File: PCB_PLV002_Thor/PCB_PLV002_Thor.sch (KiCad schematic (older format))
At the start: 24 parts, among them J1 Conn_01x12, U1 R-78B12-2.0, U2 LM317DCYRG3, U3 SN65HVD232

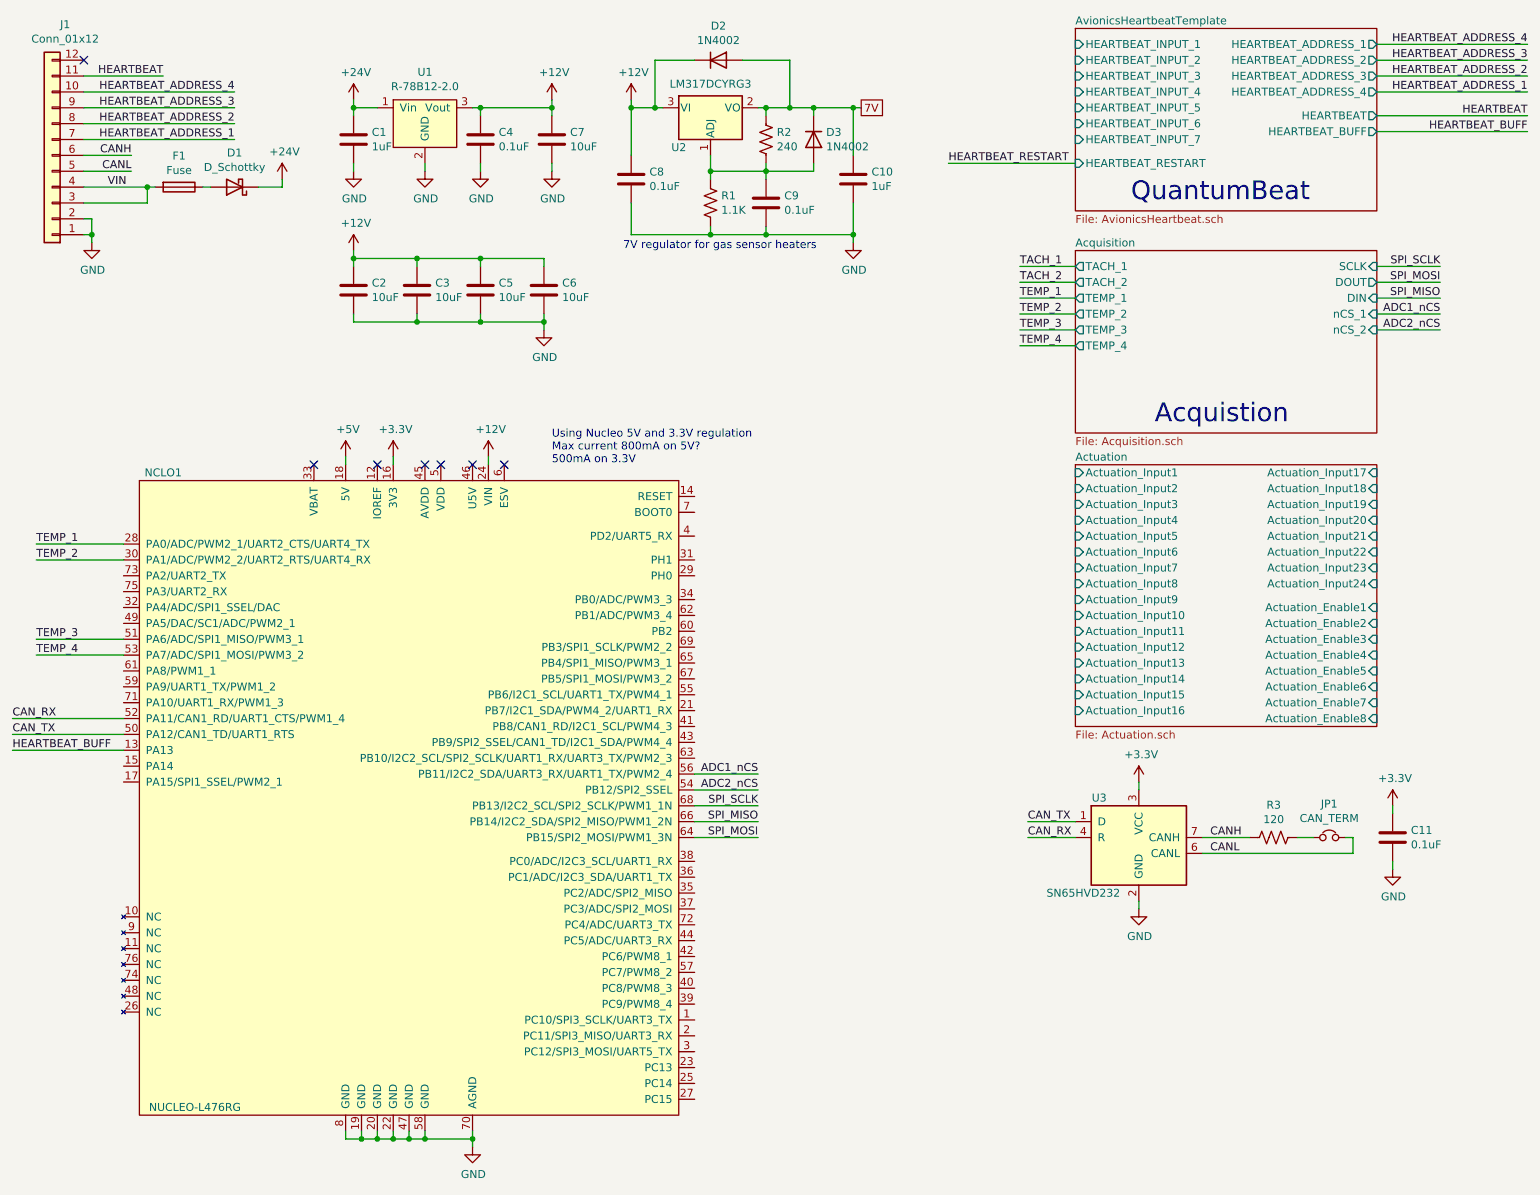
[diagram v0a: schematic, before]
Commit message: Finish schematic
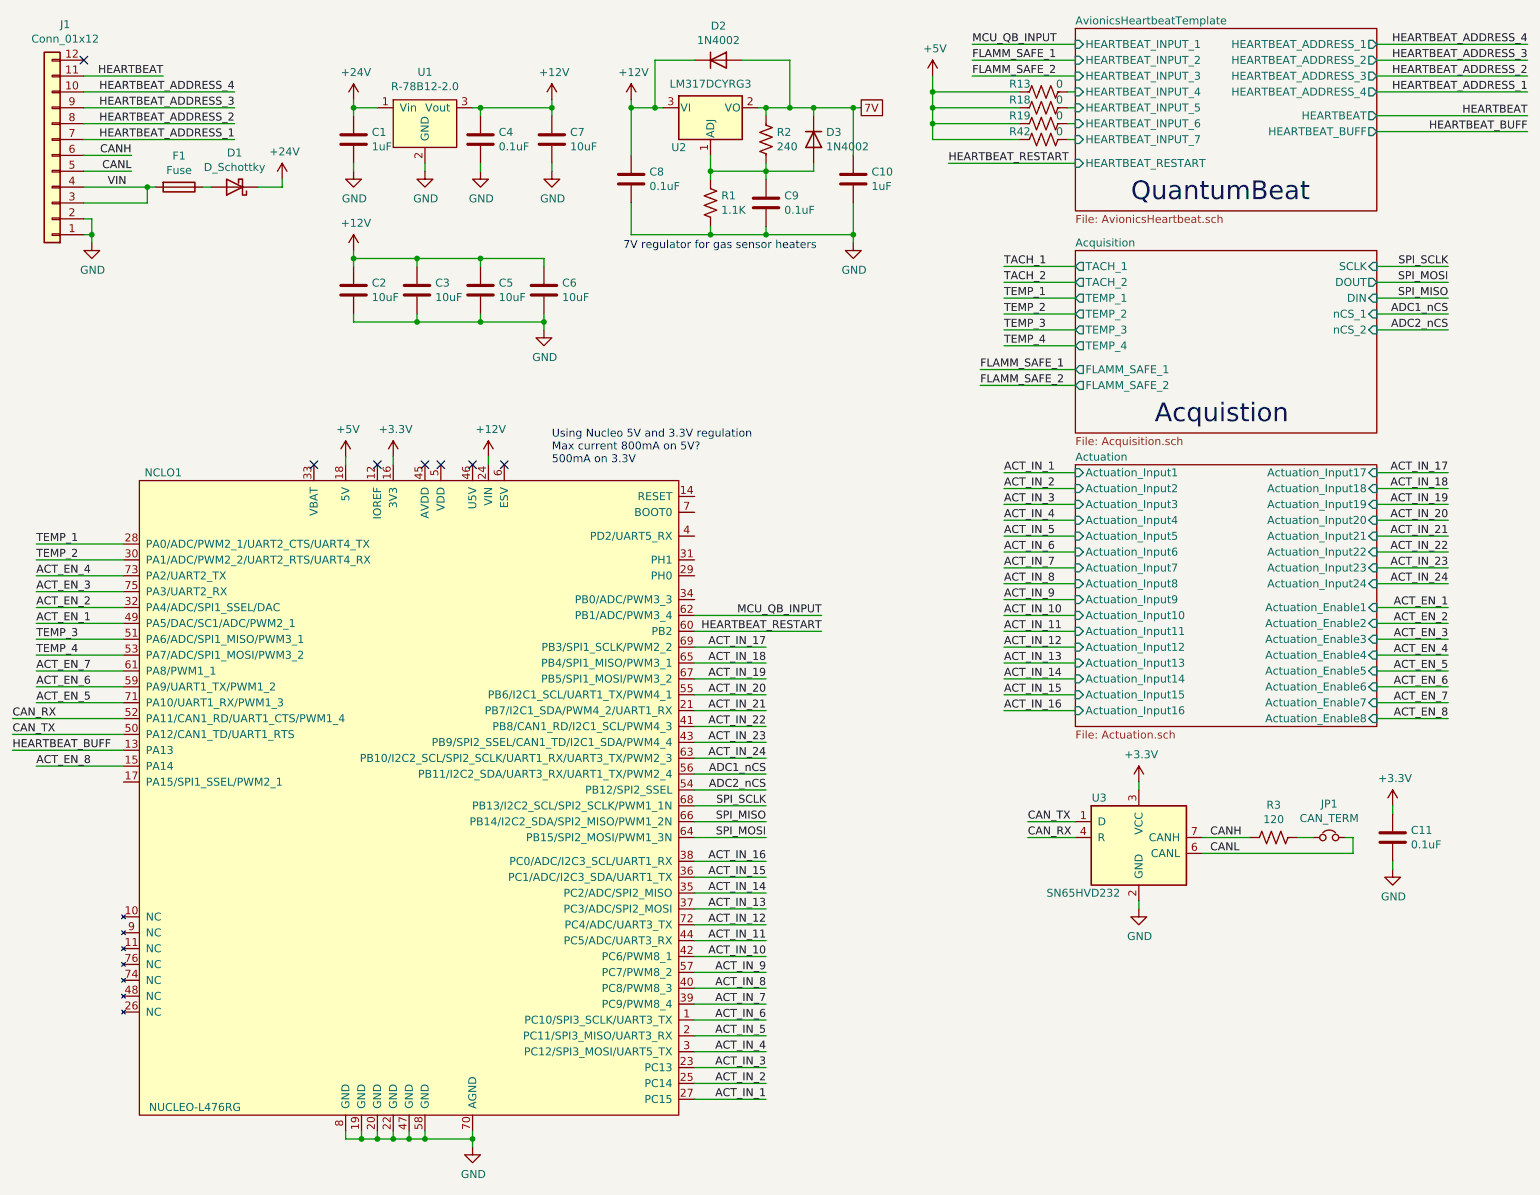
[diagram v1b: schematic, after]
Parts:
- added R13, R18, R19, R42: 0, symbol Device:R_US
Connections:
- net +5V: now also R13.2, R18.2, R19.2, R42.2
- net AvionicsHeartbeatTemplate/HEARTBEAT_INPUT_4: now also R13.1
- net AvionicsHeartbeatTemplate/HEARTBEAT_INPUT_5: now also R18.1
- net AvionicsHeartbeatTemplate/HEARTBEAT_INPUT_6: now also R19.1
- net AvionicsHeartbeatTemplate/HEARTBEAT_INPUT_7: now also R42.1
- net HEARTBEAT_RESTART: now also NCLO1.60 (PB2)
- net ACT_IN_6: now reaches NCLO1.1 (PC10/SPI3_SCLK/UART3_TX)
- net ACT_EN_8: now reaches NCLO1.15 (PA14)
- net ACT_IN_5: now reaches NCLO1.2 (PC11/SPI3_MISO/UART3_RX)
- net ACT_IN_21: now reaches NCLO1.21 (PB7/I2C1_SDA/PWM4_2/UART1_RX)
- net ACT_IN_3: now reaches NCLO1.23 (PC13)
- net ACT_IN_2: now reaches NCLO1.25 (PC14)
- net ACT_IN_1: now reaches NCLO1.27 (PC15)
- net ACT_IN_4: now reaches NCLO1.3 (PC12/SPI3_MOSI/UART5_TX)
- net ACT_EN_2: now reaches NCLO1.32 (PA4/ADC/SPI1_SSEL/DAC)
- net ACT_IN_14: now reaches NCLO1.35 (PC2/ADC/SPI2_MISO)
- net ACT_IN_15: now reaches NCLO1.36 (PC1/ADC/I2C3_SDA/UART1_TX)
- net ACT_IN_13: now reaches NCLO1.37 (PC3/ADC/SPI2_MOSI)
- net ACT_IN_16: now reaches NCLO1.38 (PC0/ADC/I2C3_SCL/UART1_RX)
- net ACT_IN_7: now reaches NCLO1.39 (PC9/PWM8_4)
- net ACT_IN_8: now reaches NCLO1.40 (PC8/PWM8_3)
- net ACT_IN_22: now reaches NCLO1.41 (PB8/CAN1_RD/I2C1_SCL/PWM4_3)
- net ACT_IN_10: now reaches NCLO1.42 (PC6/PWM8_1)
- net ACT_IN_23: now reaches NCLO1.43 (PB9/SPI2_SSEL/CAN1_TD/I2C1_SDA/PWM4_4)
- net ACT_IN_11: now reaches NCLO1.44 (PC5/ADC/UART3_RX)
- net ACT_EN_1: now reaches NCLO1.49 (PA5/DAC/SC1/ADC/PWM2_1)
- net ACT_IN_20: now reaches NCLO1.55 (PB6/I2C1_SCL/UART1_TX/PWM4_1)
- net ACT_IN_9: now reaches NCLO1.57 (PC7/PWM8_2)
- net ACT_EN_6: now reaches NCLO1.59 (PA9/UART1_TX/PWM1_2)
- net ACT_EN_7: now reaches NCLO1.61 (PA8/PWM1_1)
- net MCU_QB_INPUT: now reaches NCLO1.62 (PB1/ADC/PWM3_4)
- net ACT_IN_24: now reaches NCLO1.63 (PB10/I2C2_SCL/SPI2_SCLK/UART1_RX/UART3_TX/PWM2_3)
- net ACT_IN_18: now reaches NCLO1.65 (PB4/SPI1_MISO/PWM3_1)
- net ACT_IN_19: now reaches NCLO1.67 (PB5/SPI1_MOSI/PWM3_2)
- net ACT_IN_17: now reaches NCLO1.69 (PB3/SPI1_SCLK/PWM2_2)
- net ACT_EN_5: now reaches NCLO1.71 (PA10/UART1_RX/PWM1_3)
- net ACT_IN_12: now reaches NCLO1.72 (PC4/ADC/UART3_TX)
- net ACT_EN_4: now reaches NCLO1.73 (PA2/UART2_TX)
- net ACT_EN_3: now reaches NCLO1.75 (PA3/UART2_RX)

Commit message: Done
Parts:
- D1: footprint (none) -> BoringFootprints:DO-221AC
- D2, D3: footprint (none) -> Package_TO_SOT_SMD:SOT-23_Handsoldering
- F1: footprint (none) -> BoringFootprints:BelFuse_0679H
- J1: footprint (none) -> Connector_Molex:Molex_Micro-Fit_3.0_43045-1200_2x06_P3.00mm_Horizontal
- JP1: footprint (none) -> Jumper:SolderJumper-2_P1.3mm_Open_RoundedPad1.0x1.5mm
- R1, R2: footprint (none) -> Resistor_SMD:R_0603_1608Metric_Pad1.05x0.95mm_HandSolder
- R3: renamed from R13; footprint (none) -> Resistor_SMD:R_0603_1608Metric_Pad1.05x0.95mm_HandSolder
- R4: renamed from R18; footprint (none) -> Resistor_SMD:R_0603_1608Metric_Pad1.05x0.95mm_HandSolder
- R5: renamed from R19; footprint (none) -> Resistor_SMD:R_0603_1608Metric_Pad1.05x0.95mm_HandSolder
- R6: renamed from R42; footprint (none) -> Resistor_SMD:R_0603_1608Metric_Pad1.05x0.95mm_HandSolder
- renumbered R3 to R7
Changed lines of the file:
@@
 EESchema Schematic File Version 4
 LIBS:PCB_PLV002_Thor-cache
-EELAYER 30 0
+EELAYER 29 0
 EELAYER END
 $Descr USLetter 11000 8500
@@
 	7150 5850 7450 5850
 $Comp
-L Device:R_US R3
+L Device:R_US R7
 U 1 1 5FB52878
 P 8700 5850
-F 0 "R3" V 8495 5850 50  0000 C CNN
+F 0 "R7" V 8495 5850 50  0000 C CNN
 F 1 "120" V 8586 5850 50  0000 C CNN
 F 2 "Resistor_SMD:R_1210_3225Metric_Pad1.42x2.65mm_HandSolder" V 8740 5840 50  0001 C CNN
@@
 F 0 "JP1" H 9050 6062 50  0000 C CNN
 F 1 "CAN_TERM" H 9050 5971 50  0000 C CNN
-F 2 "" H 9050 5850 50  0001 C CNN
+F 2 "Jumper:SolderJumper-2_P1.3mm_Open_RoundedPad1.0x1.5mm" H 9050 5850 50  0001 C CNN
 F 3 "~" H 9050 5850 50  0001 C CNN
 	1    9050 5850
@@
 CANL
 $Comp
-L power:+3.3V #PWR017
+L power:+3.3V #PWR018
 U 1 1 5FB56159
 P 7850 5500
-F 0 "#PWR017" H 7850 5350 50  0001 C CNN
+F 0 "#PWR018" H 7850 5350 50  0001 C CNN
 F 1 "+3.3V" H 7865 5673 50  0000 C CNN
 F 2 "" H 7850 5500 50  0001 C CNN
@@
 	7850 6250 7850 6300
 $Comp
-L power:GND #PWR018
+L power:GND #PWR019
 U 1 1 5FB56C50
 P 7850 6300
-F 0 "#PWR018" H 7850 6050 50  0001 C CNN
+F 0 "#PWR019" H 7850 6050 50  0001 C CNN
 F 1 "GND" H 7855 6127 50  0000 C CNN
 F 2 "" H 7850 6300 50  0001 C CNN
@@
 $EndComp
 $Comp
-L power:+3.3V #PWR019
+L power:+3.3V #PWR020
 U 1 1 5FB575C6
 P 9450 5650
-F 0 "#PWR019" H 9450 5500 50  0001 C CNN
+F 0 "#PWR020" H 9450 5500 50  0001 C CNN
 F 1 "+3.3V" H 9465 5823 50  0000 C CNN
 F 2 "" H 9450 5650 50  0001 C CNN
@@
 $EndComp
 $Comp
-L power:GND #PWR020
+L power:GND #PWR021
 U 1 1 5FB57C14
 P 9450 6050
-F 0 "#PWR020" H 9450 5800 50  0001 C CNN
+F 0 "#PWR021" H 9450 5800 50  0001 C CNN
 F 1 "GND" H 9455 5877 50  0000 C CNN
 F 2 "" H 9450 6050 50  0001 C CNN
@@
 F 0 "J1" H 918 725 50  0000 C CNN
 F 1 "Conn_01x12" H 918 816 50  0000 C CNN
-F 2 "" H 1000 1550 50  0001 C CNN
+F 2 "Connector_Molex:Molex_Micro-Fit_3.0_43045-1200_2x06_P3.00mm_Horizontal" H 1000 1550 50  0001 C CNN
 F 3 "~" H 1000 1550 50  0001 C CNN
 	1    1000 1550
@@
 F 0 "F1" V 1603 1750 50  0000 C CNN
 F 1 "Fuse" V 1694 1750 50  0000 C CNN
-F 2 "" V 1730 1750 50  0001 C CNN
+F 2 "BoringFootprints:BelFuse_0679H" V 1730 1750 50  0001 C CNN
 F 3 "~" H 1800 1750 50  0001 C CNN
 	1    1800 1750
@@
 F 0 "D1" H 2150 1534 50  0000 C CNN
 F 1 "D_Schottky" H 2150 1625 50  0000 C CNN
-F 2 "" H 2150 1750 50  0001 C CNN
+F 2 "BoringFootprints:DO-221AC" H 2150 1750 50  0001 C CNN
 F 3 "~" H 2150 1750 50  0001 C CNN
 	1    2150 1750
@@
 F 0 "R2" H 5568 1496 50  0000 L CNN
 F 1 "240" H 5568 1405 50  0000 L CNN
-F 2 "" V 5540 1440 50  0001 C CNN
+F 2 "Resistor_SMD:R_0603_1608Metric_Pad1.05x0.95mm_HandSolder" V 5540 1440 50  0001 C CNN
 F 3 "~" H 5500 1450 50  0001 C CNN
 	1    5500 1450
@@
 F 0 "R1" H 5218 1896 50  0000 L CNN
 F 1 "1.1K" H 5218 1805 50  0000 L CNN
-F 2 "" V 5190 1840 50  0001 C CNN
+F 2 "Resistor_SMD:R_0603_1608Metric_Pad1.05x0.95mm_HandSolder" V 5190 1840 50  0001 C CNN
 F 3 "~" H 5150 1850 50  0001 C CNN
 	1    5150 1850
@@
 F 0 "D2" H 5200 1166 50  0000 C CNN
 F 1 "1N4002" H 5200 1075 50  0000 C CNN
-F 2 "" H 5200 950 50  0001 C CNN
+F 2 "Package_TO_SOT_SMD:SOT-23_Handsoldering" H 5200 950 50  0001 C CNN
 F 3 "~" H 5200 950 50  0001 C CNN
 	1    5200 950
@@
 F 0 "D3" V 5754 1529 50  0000 L CNN
 F 1 "1N4002" V 5845 1529 50  0000 L CNN
-F 2 "" H 5800 1450 50  0001 C CNN
+F 2 "Package_TO_SOT_SMD:SOT-23_Handsoldering" H 5800 1450 50  0001 C CNN
 F 3 "~" H 5800 1450 50  0001 C CNN
 	1    5800 1450
@@
 FLAMM_SAFE_2
 $Comp
-L Device:R_US R13
+L Device:R_US R3
 U 1 1 603DA7D2
 P 7250 1150
-F 0 "R13" V 7200 1000 50  0000 C CNN
+F 0 "R3" V 7200 1000 50  0000 C CNN
 F 1 "0" V 7200 1250 50  0000 C CNN
-F 2 "" V 7290 1140 50  0001 C CNN
+F 2 "Resistor_SMD:R_0603_1608Metric_Pad1.05x0.95mm_HandSolder" V 7290 1140 50  0001 C CNN
 F 3 "~" H 7250 1150 50  0001 C CNN
 	1    7250 1150
@@
 	6550 1150 6550 1050
 $Comp
-L Device:R_US R18
+L Device:R_US R4
 U 1 1 603F58C2
 P 7250 1250
-F 0 "R18" V 7200 1100 50  0000 C CNN
+F 0 "R4" V 7200 1100 50  0000 C CNN
 F 1 "0" V 7200 1350 50  0000 C CNN
-F 2 "" V 7290 1240 50  0001 C CNN
+F 2 "Resistor_SMD:R_0603_1608Metric_Pad1.05x0.95mm_HandSolder" V 7290 1240 50  0001 C CNN
 F 3 "~" H 7250 1250 50  0001 C CNN
 	1    7250 1250
@@
 $EndComp
 $Comp
-L Device:R_US R19
+L Device:R_US R5
 U 1 1 603F5D33
 P 7250 1350
-F 0 "R19" V 7200 1200 50  0000 C CNN
+F 0 "R5" V 7200 1200 50  0000 C CNN
 F 1 "0" V 7200 1450 50  0000 C CNN
-F 2 "" V 7290 1340 50  0001 C CNN
+F 2 "Resistor_SMD:R_0603_1608Metric_Pad1.05x0.95mm_HandSolder" V 7290 1340 50  0001 C CNN
 F 3 "~" H 7250 1350 50  0001 C CNN
 	1    7250 1350
@@
 $EndComp
 $Comp
-L Device:R_US R42
+L Device:R_US R6
 U 1 1 603F5F43
 P 7250 1450
-F 0 "R42" V 7200 1300 50  0000 C CNN
+F 0 "R6" V 7200 1300 50  0000 C CNN
 F 1 "0" V 7200 1550 50  0000 C CNN
-F 2 "" V 7290 1440 50  0001 C CNN
+F 2 "Resistor_SMD:R_0603_1608Metric_Pad1.05x0.95mm_HandSolder" V 7290 1440 50  0001 C CNN
 F 3 "~" H 7250 1450 50  0001 C CNN
 	1    7250 1450
@@
 	6550 1350 6550 1250
 $Comp
-L power:+5V #PWR030
+L power:+5V #PWR017
 U 1 1 604570BE
 P 6550 1050
-F 0 "#PWR030" H 6550 900 50  0001 C CNN
+F 0 "#PWR017" H 6550 900 50  0001 C CNN
 F 1 "+5V" H 6565 1223 50  0000 C CNN
 F 2 "" H 6550 1050 50  0001 C CNN

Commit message: Schematic fix of actuator drivers
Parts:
- NCLO1: symbol boringlib:NUCLEO-L476RG -> PCB_PLV002_Thor-rescue:NUCLEO-L476RG-boringlib
- U1: symbol boringlib:R-78B12-2.0 -> PCB_PLV002_Thor-rescue:R-78B12-2.0-boringlib
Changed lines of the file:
@@
 EESchema Schematic File Version 4
-LIBS:PCB_PLV002_Thor-cache
-EELAYER 29 0
+EELAYER 30 0
 EELAYER END
 $Descr USLetter 11000 8500
@@
 QuantumBeat
 $Comp
-L boringlib:NUCLEO-L476RG NCLO1
+L PCB_PLV002_Thor-rescue:NUCLEO-L476RG-boringlib NCLO1
 U 1 1 5FB4B31E
 P 3250 5600
@@
 Acquistion
 $Comp
-L boringlib:R-78B12-2.0 U1
+L PCB_PLV002_Thor-rescue:R-78B12-2.0-boringlib U1
 U 1 1 5FC3CFC1
 P 3350 1350
